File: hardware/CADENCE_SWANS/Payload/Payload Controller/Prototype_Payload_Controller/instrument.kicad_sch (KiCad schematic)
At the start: 11 parts, among them J1 Conn_01x06_Pin, J10 Conn_01x03, J2 Conn_01x06_Pin, J3 Conn_01x06_Pin, J4 Conn_01x06_Pin, J5 Conn_Coaxial, J6 Conn_Coaxial, J7 Conn_Coaxial, J8 Conn_Coaxial

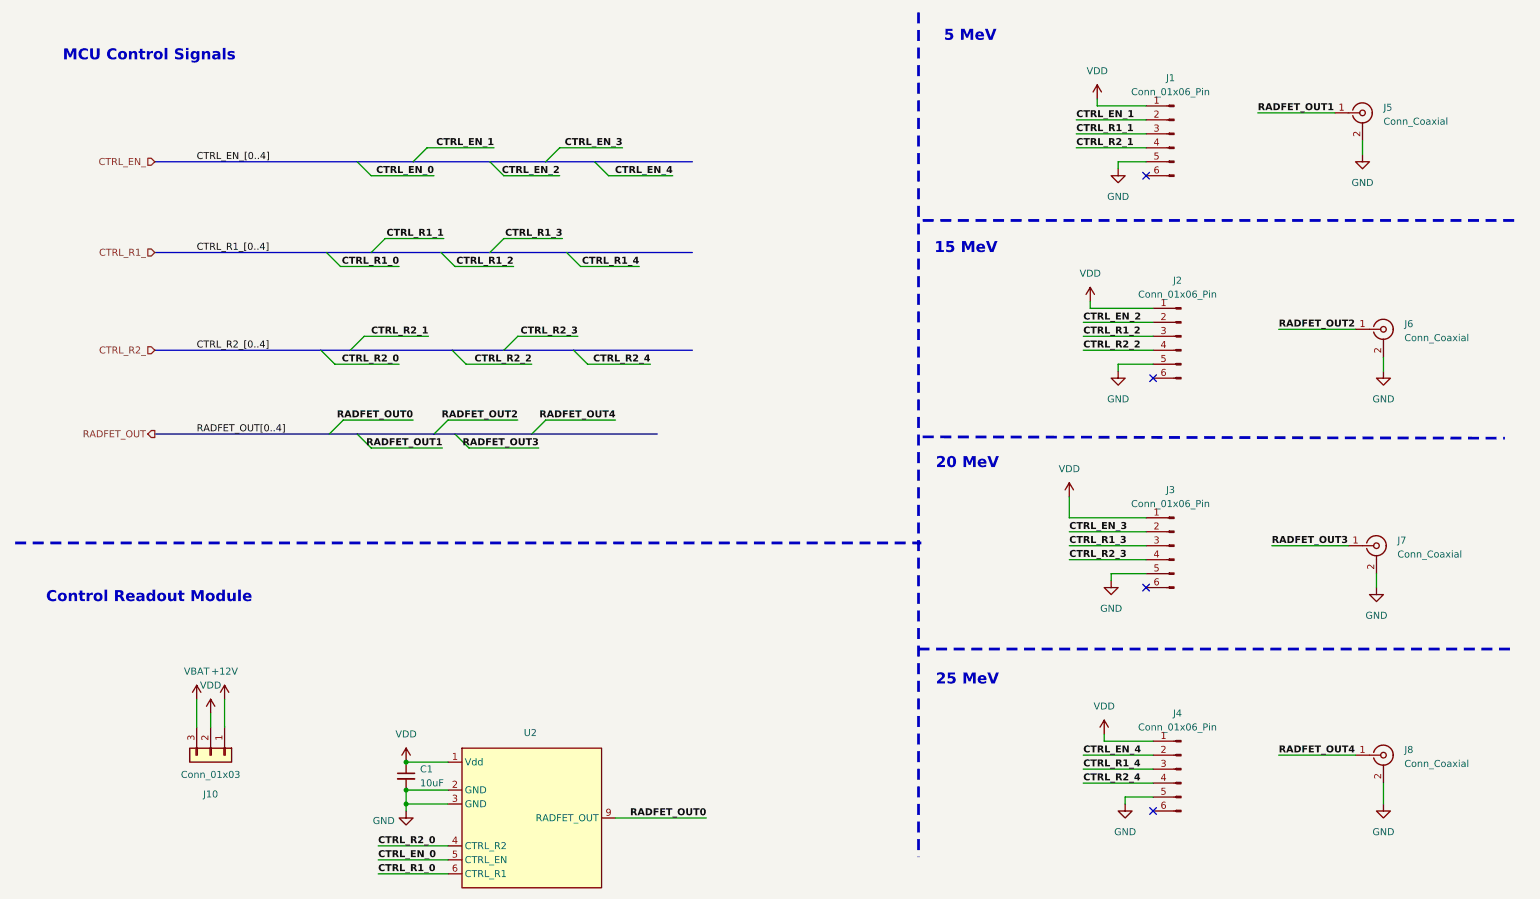
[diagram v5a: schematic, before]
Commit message: resolved bus naming issues
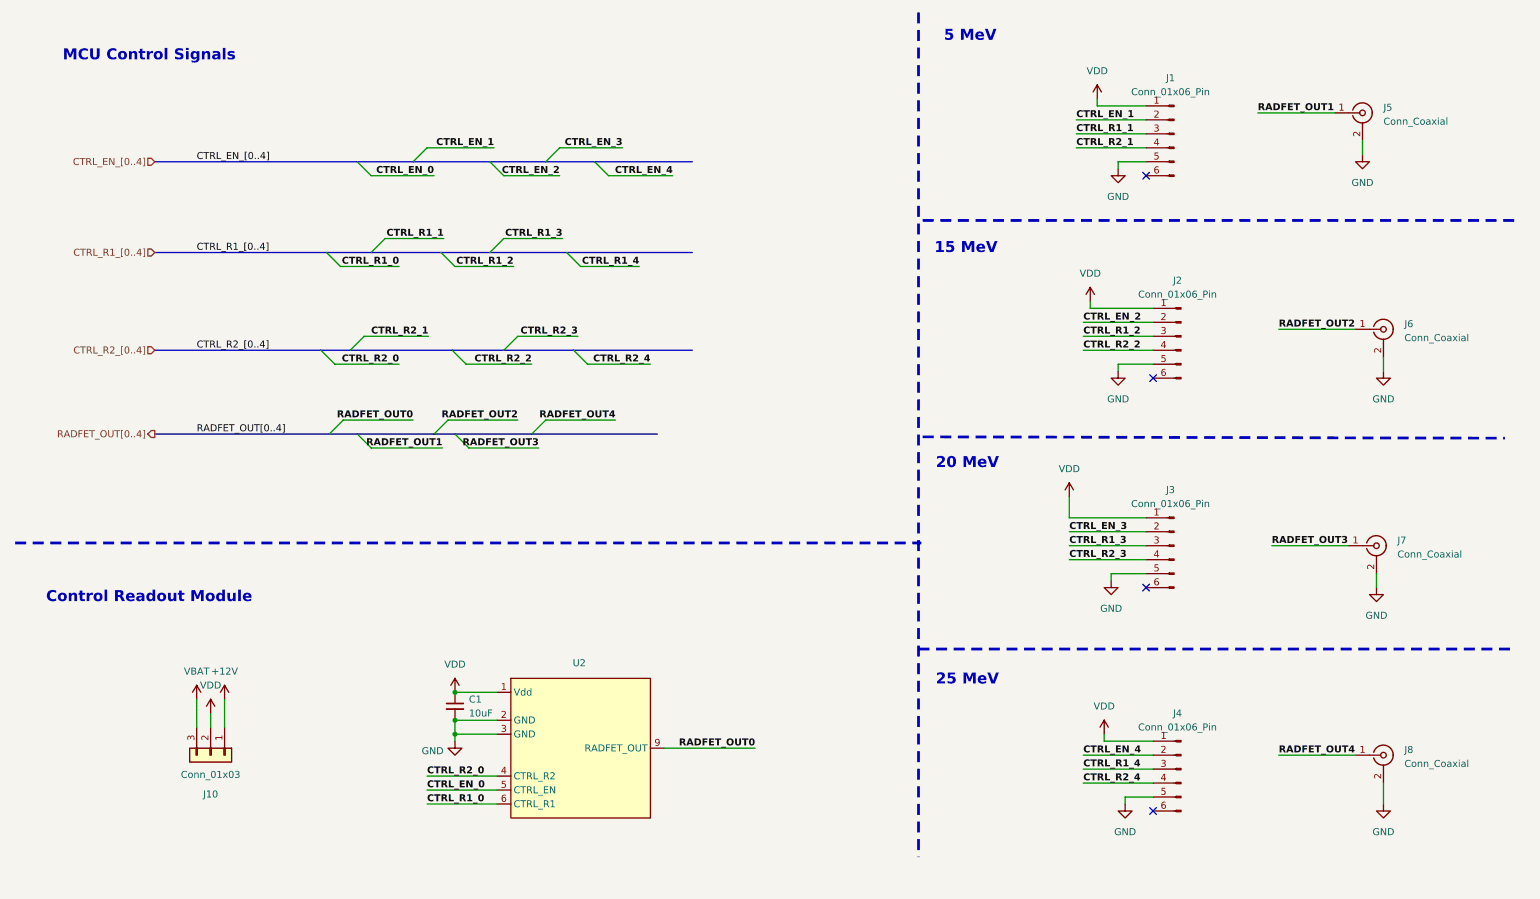
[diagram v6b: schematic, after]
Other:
- moved on the sheet: C1, U2
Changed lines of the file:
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@@
 	)
 	(junction
-		(at 83.82 156.21)
+		(at 92.71 143.51)
 		(diameter 0)
 		(color 0 0 0 0)
 	)
 	(junction
-		(at 83.82 153.67)
+		(at 92.71 140.97)
 		(diameter 0)
 		(color 0 0 0 0)
 	)
 	(junction
-		(at 83.82 148.59)
+		(at 92.71 135.89)
 		(diameter 0)
 		(color 0 0 0 0)
@@
 	(wire
 		(pts
-			(xy 83.82 153.67) (xy 91.44 153.67)
+			(xy 92.71 140.97) (xy 100.33 140.97)
 		)
 		(stroke
@@
 	(wire
 		(pts
-			(xy 78.74 166.37) (xy 91.44 166.37)
+			(xy 87.63 153.67) (xy 100.33 153.67)
 		)
 		(stroke
@@
 	(wire
 		(pts
-			(xy 83.82 153.67) (xy 83.82 156.21)
+			(xy 92.71 140.97) (xy 92.71 143.51)
 		)
 		(stroke
@@
 	(wire
 		(pts
-			(xy 83.82 156.21) (xy 83.82 157.48)
+			(xy 92.71 143.51) (xy 92.71 144.78)
 		)
 		(stroke
@@
 	(wire
 		(pts
-			(xy 78.74 163.83) (xy 91.44 163.83)
+			(xy 87.63 151.13) (xy 100.33 151.13)
 		)
 		(stroke
@@
 	(wire
 		(pts
-			(xy 83.82 156.21) (xy 91.44 156.21)
+			(xy 92.71 143.51) (xy 100.33 143.51)
 		)
 		(stroke
@@
 	(wire
 		(pts
-			(xy 83.82 148.59) (xy 91.44 148.59)
+			(xy 92.71 135.89) (xy 100.33 135.89)
 		)
 		(stroke
@@
 	(wire
 		(pts
-			(xy 121.92 158.75) (xy 138.43 158.75)
+			(xy 130.81 146.05) (xy 147.32 146.05)
 		)
 		(stroke
@@
 	(wire
 		(pts
-			(xy 78.74 168.91) (xy 91.44 168.91)
+			(xy 87.63 156.21) (xy 100.33 156.21)
 		)
 		(stroke
@@
 	)
 	(label "CTRL_R2_0"
-		(at 78.74 163.83 0)
+		(at 87.63 151.13 0)
 		(effects
 			(font
@@
 	)
 	(label "CTRL_EN_0"
-		(at 78.74 166.37 0)
+		(at 87.63 153.67 0)
 		(effects
 			(font
@@
 	)
 	(label "CTRL_R1_0"
-		(at 78.74 168.91 0)
+		(at 87.63 156.21 0)
 		(effects
 			(font
@@
 	)
 	(label "RADFET_OUT0"
-		(at 138.43 158.75 180)
+		(at 147.32 146.05 180)
 		(effects
 			(font
@@
 		)
 	)
-	(hierarchical_label "RADFET_OUT"
+	(hierarchical_label "RADFET_OUT[0..4]"
 		(shape output)
 		(at 38.1 88.9 180)
@@
 		)
 	)
-	(hierarchical_label "CTRL_R1_"
+	(hierarchical_label "CTRL_R1_[0..4]"
 		(shape input)
 		(at 38.1 55.88 180)
@@
 		)
 	)
-	(hierarchical_label "CTRL_EN_"
+	(hierarchical_label "CTRL_EN_[0..4]"
 		(shape input)
 		(at 38.1 39.37 180)
@@
 		)
 	)
-	(hierarchical_label "CTRL_R2_"
+	(hierarchical_label "CTRL_R2_[0..4]"
 		(shape input)
 		(at 38.1 73.66 180)
@@
 	(symbol
 		(lib_id "Device:C_Small")
-		(at 83.82 151.13 0)
+		(at 92.71 138.43 0)
 		(unit 1)
 		(exclude_from_sim no)
@@
 		(dnp no)
 		(property "Reference" "C1"
-			(at 86.36 149.8662 0)
+			(at 95.25 137.1662 0)
 			(effects
 				(font
@@
 		)
 		(property "Value" "10uF"
-			(at 86.36 152.4 0)
+			(at 95.25 139.7 0)
 			(effects
 				(font
@@
 		)
 		(property "Footprint" ""
-			(at 83.82 151.13 0)
+			(at 92.71 138.43 0)
 			(effects
 				(font
@@
 		)
 		(property "Datasheet" "~"
-			(at 83.82 151.13 0)
+			(at 92.71 138.43 0)
 			(effects
 				(font
@@
 		)
 		(property "Description" "Unpolarized capacitor, small symbol"
-			(at 83.82 151.13 0)
+			(at 92.71 138.43 0)
 			(effects
 				(font
@@
 	(symbol
 		(lib_id "power:VDD")
-		(at 83.82 148.59 0)
+		(at 92.71 135.89 0)
 		(unit 1)
 		(exclude_from_sim no)
@@
 		(fields_autoplaced yes)
 		(property "Reference" "#PWR041"
-			(at 83.82 152.4 0)
+			(at 92.71 139.7 0)
 			(effects
 				(font
@@
 		)
 		(property "Value" "VDD"
-			(at 83.82 143.51 0)
+			(at 92.71 130.81 0)
 			(effects
 				(font
@@
 		)
 		(property "Footprint" ""
-			(at 83.82 148.59 0)
+			(at 92.71 135.89 0)
 			(effects
 				(font
@@
 		)
 		(property "Datasheet" ""
-			(at 83.82 148.59 0)
+			(at 92.71 135.89 0)
 			(effects
 				(font
@@
 		)
 		(property "Description" "Power symbol creates a global label with name \"VDD\""
-			(at 83.82 148.59 0)
+			(at 92.71 135.89 0)
 			(effects
 				(font
@@
 	(symbol
 		(lib_id "power:GND")
-		(at 83.82 157.48 0)
+		(at 92.71 144.78 0)
 		(unit 1)
 		(exclude_from_sim no)
@@
 		(dnp no)
 		(property "Reference" "#PWR013"
-			(at 83.82 163.83 0)
+			(at 92.71 151.13 0)
 			(effects
 				(font
@@
 		)
 		(property "Value" "GND"
-			(at 79.756 159.258 0)
+			(at 88.646 146.558 0)
 			(effects
 				(font
@@
 		)
 		(property "Footprint" ""
-			(at 83.82 157.48 0)
+			(at 92.71 144.78 0)
 			(effects
 				(font
@@
 		)
 		(property "Datasheet" ""
-			(at 83.82 157.48 0)
+			(at 92.71 144.78 0)
 			(effects
 				(font
@@
 		)
 		(property "Description" "Power symbol creates a global label with name \"GND\" , ground"
-			(at 83.82 157.48 0)
+			(at 92.71 144.78 0)
 			(effects
 				(font
@@
 	(symbol
 		(lib_id "VT01-RM:RM_VT01_A_RADFET Readout Module")
-		(at 93.98 171.45 0)
+		(at 102.87 158.75 0)
 		(unit 1)
 		(exclude_from_sim no)
@@
 		(dnp no)
 		(property "Reference" "U2"
-			(at 106.426 143.256 0)
+			(at 115.316 130.556 0)
 			(effects
 				(font
@@
 		)
 		(property "Value" "~"
-			(at 106.68 144.78 0)
+			(at 115.57 132.08 0)
 			(effects
 				(font
@@
 		)
 		(property "Footprint" ""
-			(at 93.98 171.45 0)
+			(at 102.87 158.75 0)
 			(effects
 				(font
@@
 		)
 		(property "Datasheet" ""
-			(at 93.98 171.45 0)
+			(at 102.87 158.75 0)
 			(effects
 				(font
@@
 		)
 		(property "Description" ""
-			(at 93.98 171.45 0)
+			(at 102.87 158.75 0)
 			(effects
 				(font

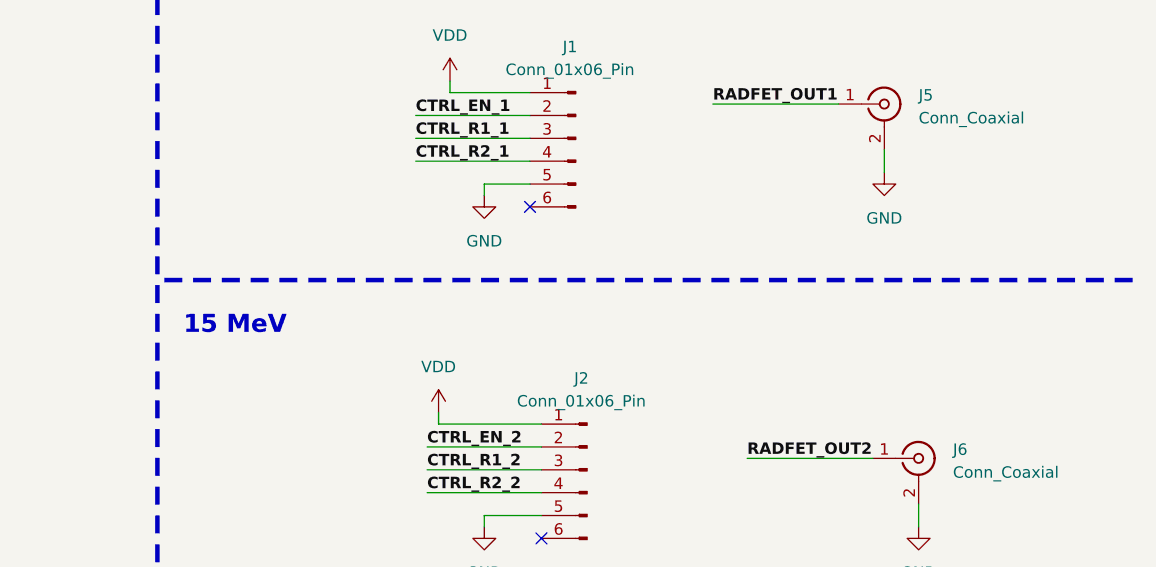
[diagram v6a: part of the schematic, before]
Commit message: cleaned up schematics and assigned footprints for resistors and capacitors
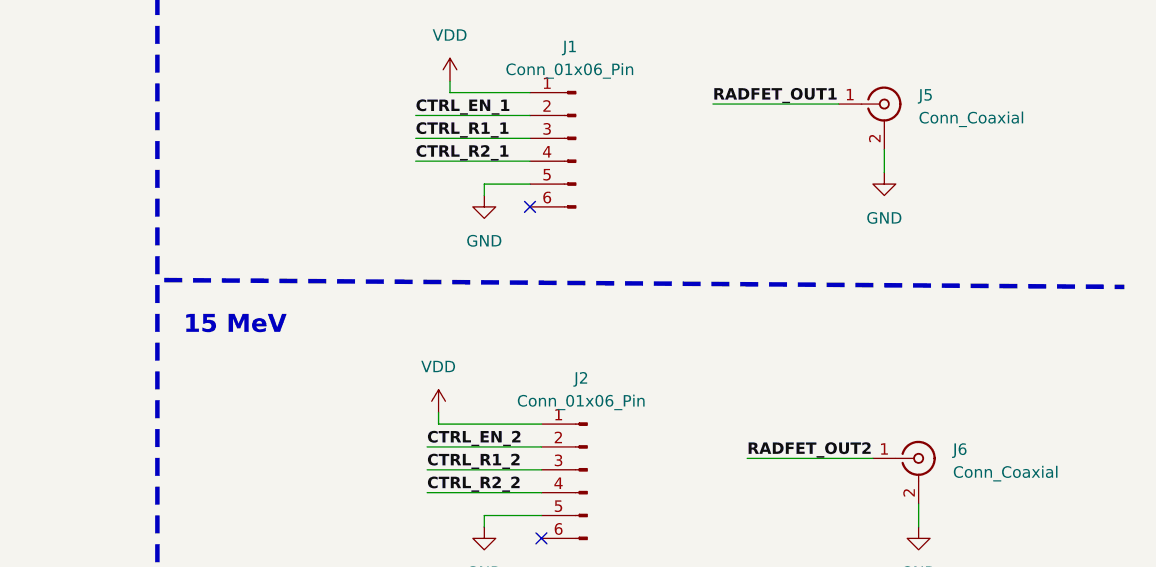
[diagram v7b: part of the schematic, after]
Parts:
- C1: footprint (none) -> Capacitor_SMD:C_0603_1608Metric
- J5, J6, J7, J8: footprint (none) -> Connector_Coaxial:SMA_Amphenol_901-144_Vertical
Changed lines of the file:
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@@
 	(polyline
 		(pts
-			(xy 177.8 50.038) (xy 285.75 50.038)
+			(xy 177.8 50.038) (xy 284.48 50.8)
 		)
 		(stroke
@@
 			)
 		)
-		(property "Footprint" ""
+		(property "Footprint" "Connector_Coaxial:SMA_Amphenol_901-144_Vertical"
 			(at 260.35 109.22 0)
 			(effects
@@
 			)
 		)
-		(property "Footprint" ""
+		(property "Footprint" "Connector_Coaxial:SMA_Amphenol_901-144_Vertical"
 			(at 261.62 69.85 0)
 			(effects
@@
 			)
 		)
-		(property "Footprint" ""
+		(property "Footprint" "Capacitor_SMD:C_0603_1608Metric"
 			(at 92.71 138.43 0)
 			(effects
@@
 			)
 		)
-		(property "Footprint" ""
+		(property "Footprint" "Connector_Coaxial:SMA_Amphenol_901-144_Vertical"
 			(at 261.62 147.32 0)
 			(effects
@@
 			)
 		)
-		(property "Footprint" ""
+		(property "Footprint" "Connector_Coaxial:SMA_Amphenol_901-144_Vertical"
 			(at 257.81 30.48 0)
 			(effects

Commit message: assigned more footprints
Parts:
- J1, J2, J3, J4: footprint (none) -> Connector_Hirose:Hirose_DF11-6DP-2DSA_2x03_P2.00mm_Vertical
- U2: footprint (none) -> VT01-RM:RM-VT01-A
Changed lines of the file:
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@@
 			)
 		)
-		(property "Footprint" ""
+		(property "Footprint" "Connector_Hirose:Hirose_DF11-6DP-2DSA_2x03_P2.00mm_Vertical"
 			(at 224.79 71.12 0)
 			(effects
@@
 			)
 		)
-		(property "Footprint" ""
+		(property "Footprint" "Connector_Hirose:Hirose_DF11-6DP-2DSA_2x03_P2.00mm_Vertical"
 			(at 223.52 109.22 0)
 			(effects
@@
 			)
 		)
-		(property "Footprint" ""
+		(property "Footprint" "Connector_Hirose:Hirose_DF11-6DP-2DSA_2x03_P2.00mm_Vertical"
 			(at 224.79 149.86 0)
 			(effects
@@
 			)
 		)
-		(property "Footprint" ""
+		(property "Footprint" "VT01-RM:RM-VT01-A"
 			(at 102.87 158.75 0)
 			(effects
@@
 			)
 		)
-		(property "Footprint" ""
+		(property "Footprint" "Connector_Hirose:Hirose_DF11-6DP-2DSA_2x03_P2.00mm_Vertical"
 			(at 223.52 34.29 0)
 			(effects
